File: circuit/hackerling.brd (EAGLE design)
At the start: 82.5 x 67.4 mm, 38 parts, among them IC1 MCP23017SP, IC2 MCP2300X/P, IC3 MIC5219BM5, SW2 SWITCH_B13EH, U1 MMA8452Q, U2 LCD-16X2NOSILK, U3 ARDUINOR3-BPLACE, U5 PCA9306, U7 POT

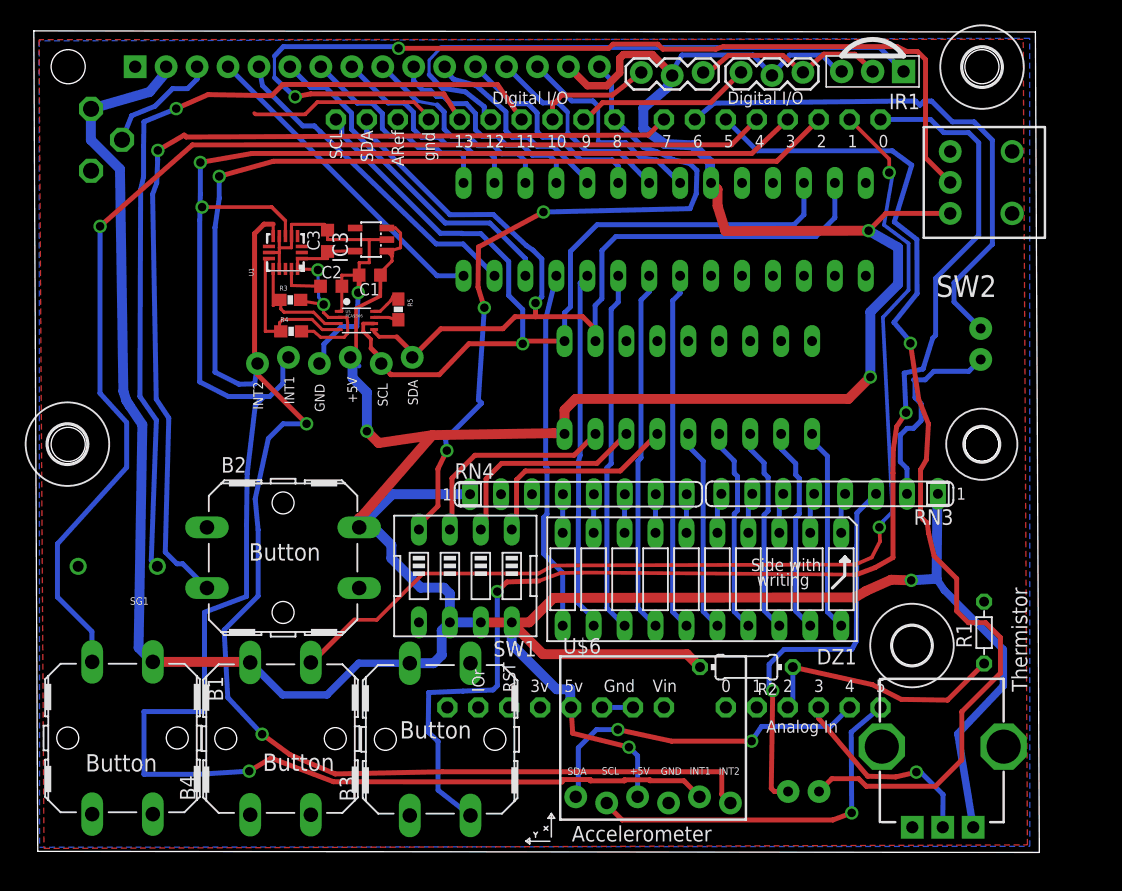
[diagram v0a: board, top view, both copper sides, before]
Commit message: changing accelerometer, adding hooked up address pins
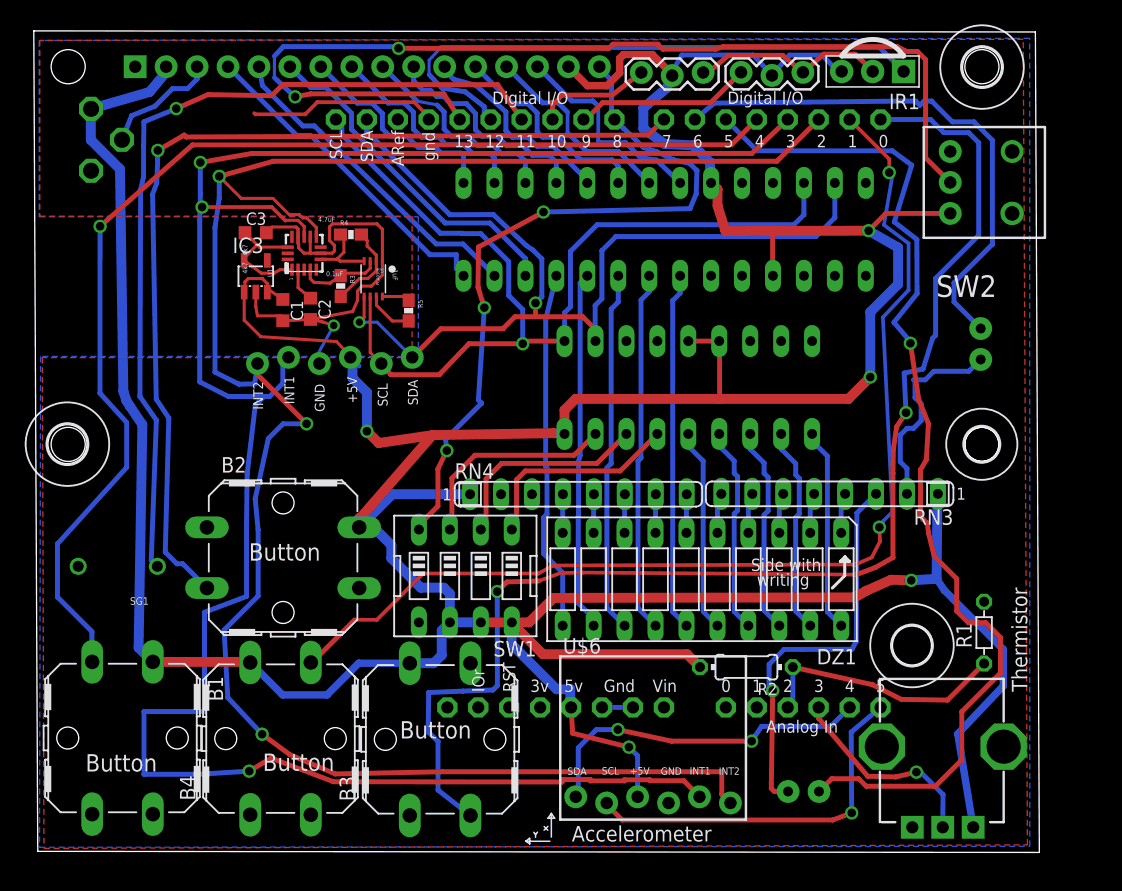
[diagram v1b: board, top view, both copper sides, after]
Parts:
- moved IC3 9.93 mm to (18.0, 48.5), turned to 0 degrees
- moved R4 9.34 mm to (25.8, 51.9)
- moved C1 7.70 mm to (20.2, 45.7), turned to 270 degrees
- moved C3 5.94 mm to (18.0, 52.0), turned to 0 degrees
- moved R3 4.29 mm to (24.9, 47.6), turned to 270 degrees
- moved U5 3.69 mm to (27.6, 48.2), turned to 180 degrees
- moved C2 2.51 mm to (22.5, 45.8), turned to 270 degrees
- moved U1 1.54 mm to (21.9, 50.3)
- moved R5 0.86 mm to (30.5, 45.6)
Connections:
- net GND: now also IC1.15, IC1.16, IC1.17, IC2.3, IC2.4
- net VCC: now also IC1.18, IC2.5, IC2.6
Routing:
- net VCC: track 379.8 -> 394.6 mm
- net SDA_3: track 13.6 -> 5.98 mm
- net GND: track 68.3 -> 74.7 mm
- net SDA: track 77.5 -> 81.4 mm, vias 1 -> 2
- net 3.3V: track 21.0 -> 17.3 mm, vias 2 -> 0
- net SCL_3: track 9.74 -> 6.79 mm
- net A_INT2: track 164.1 -> 161.7 mm
- net A_INT1: track 172.0 -> 173.7 mm
- net SCL: track 78.7 -> 80.2 mm
- net 5V: track 2.63 -> 3.90 mm
- net N$25: track 3.75 -> 2.81 mm
- net N$10: track 26.4 -> 27.1 mm
- net N$27: track 2.82 -> 2.29 mm
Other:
- board text added: "0.1uF"
- board text added: "1uF"
- board text added: "4.7uF"
- board text added: "4k7"

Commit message: adding adafruit libs to software folder
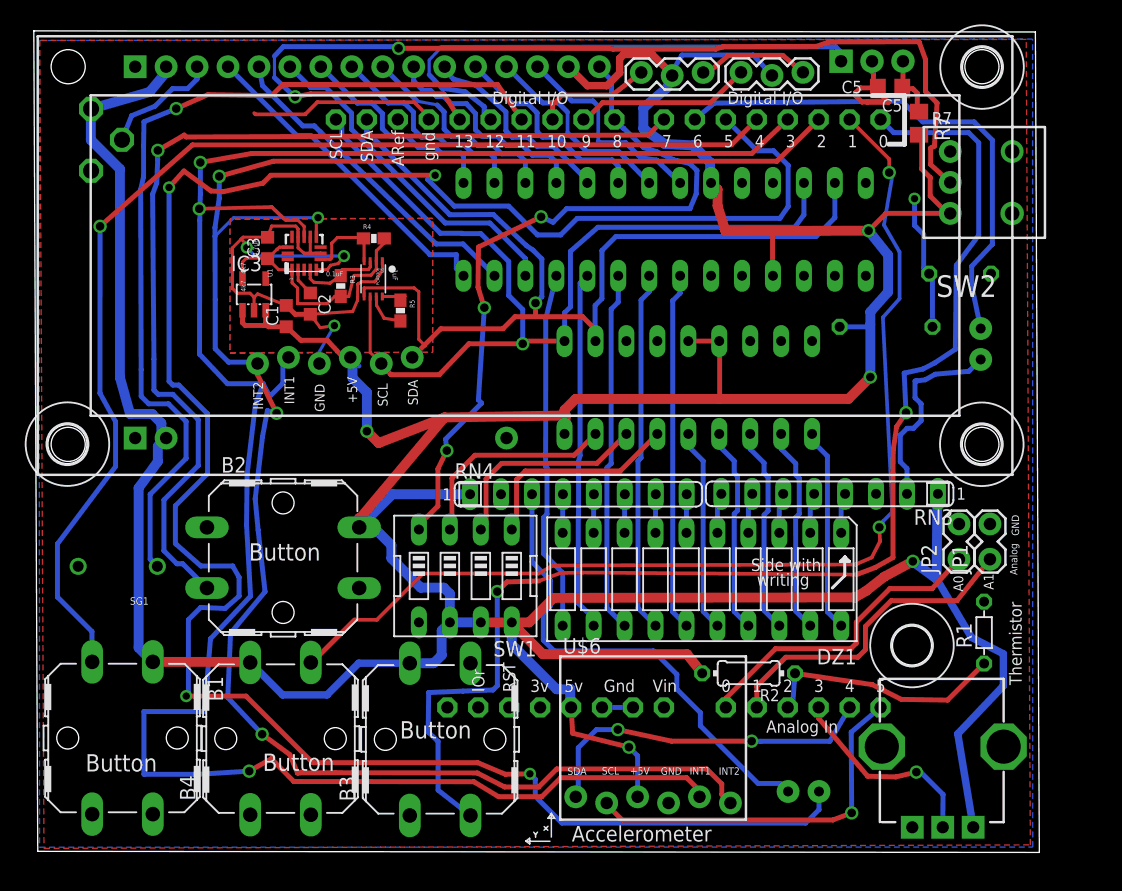
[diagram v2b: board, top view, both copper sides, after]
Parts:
- added C4: 10uF, rcl:C050-050X075
- added C5: (no value), resistor:C0805K
- added JP1, JP2: (no value), SparkFun:1X02_LOCK
- added R6: 47, resistor:0204/7
- added R7: (no value), rcl:R0805
- H1, H2, H3: value MOUNT-HOLE3.2 -> MOUNTHOLE'3.2; device holes:3,2 -> hackerscouts:HOLE_3.2
- H4: value MOUNT-HOLE2.8 -> MOUNTHOLE'3.2; device holes:2,8 -> hackerscouts:HOLE_3.2
- U2: value LCD-16X2NOSILK -> LCD_16X2; device SparkFun:LCD-16X2_NOSILK -> hackerscouts:LCD_16X2
- moved R4 1.91 mm to (27.7, 51.5)
- moved C3 1.59 mm to (18.9, 50.8), turned to 90 degrees
- moved IC3 1.50 mm to (17.8, 47.0)
- moved IR1 0.84 mm to (68.6, 66.1), flipped to the bottom
- moved R5 0.68 mm to (29.9, 45.6)
- moved C1 0.56 mm to (20.5, 45.2), turned to 90 degrees
- moved R2 0.54 mm to (58.4, 15.9)
- moved C2 0.42 mm to (22.5, 46.2)
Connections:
- new net N$19: C4.1, C5.1, IR1.3, R6.1, R7.1
- new net N$24: JP1.1, U3.A1
- new net N$26: JP2.1, U3.A0
- net GND: now also C4.2, C5.2, JP1.2, JP2.2, U2.B1
- net N$16: now also RN4.3; no longer RN3.3
- net N$2: now also U2.B13
- net VCC: now also R6.2, R7.2, U2.B2; no longer IR1.3
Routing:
- net IR_OUT1: track 86.2 -> 176.8 mm, vias 1 -> 4
- net N$24: track 0.00 -> 26.5 mm
- net N$26: track 0.00 -> 25.7 mm
- net N$19: track 0.00 -> 17.1 mm, vias 0 -> 1
- net GND: track 74.7 -> 86.6 mm, vias 1 -> 3
- net N$16: track 32.6 -> 39.4 mm, vias 1 -> 0
- net IR_IN: track 48.1 -> 43.1 mm
- net VCC: track 394.6 -> 399.5 mm
- net 3.3V: track 17.3 -> 22.0 mm
- net A_INT2: track 161.7 -> 157.3 mm, vias 3 -> 4
- net N$15: track 70.5 -> 74.5 mm
- net BTN2: track 80.5 -> 83.6 mm
- net SDA: track 81.4 -> 83.4 mm, vias 2 -> 1
- net IR_OUT2: track 44.2 -> 42.6 mm
- net BTN1: track 97.3 -> 96.1 mm
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- added copper zone on layer 1, net N$14
- added copper zone on layer 16, net N$14
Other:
- board text added: "A0"
- board text added: "A1"
- board text added: "Analog"
- board text added: "C4"
- board text added: "C5"
- board text added: "R6"
- board text added: "R7"

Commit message: old changes to circuit adding design docs adding libraries for new chips
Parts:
- added LED3: (no value), SparkFun:LED5MM
- R7: device rcl:R0805 -> rcl:R0603
- moved R7 3.78 mm to (72.5, 57.2)
- moved C5 2.61 mm to (70.6, 66.4)
- moved IR1 1.92 mm to (69.3, 64.3)
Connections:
- new net N$32: LED3.A, RN4.2
- net BTN3: now also B3.4; no longer B3.3
- net GND: now also B2.2, B3.1, SW1.6, SW1.7, SW1.8
- net IR_OUT1: now also LED3.K
- net N$3: now also U2.B12
- net VCC: no longer B1.1, B2.2, B3.2, B4.2, SW1.6, SW1.7, SW1.8
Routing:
- net VCC: track 399.5 -> 295.8 mm, vias 5 -> 4
- net N$32: track 0.00 -> 39.4 mm, vias 0 -> 3
- net BTN3: track 105.0 -> 77.2 mm
- net IR_OUT1: track 176.8 -> 185.7 mm, vias 4 -> 5
- net GND: track 86.6 -> 78.6 mm
- net N$19: track 17.1 -> 24.7 mm
- net IR_OUT2: track 42.6 -> 38.9 mm
- net IR_IN: track 43.1 -> 45.0 mm
- net N$12: track 16.6 -> 15.9 mm

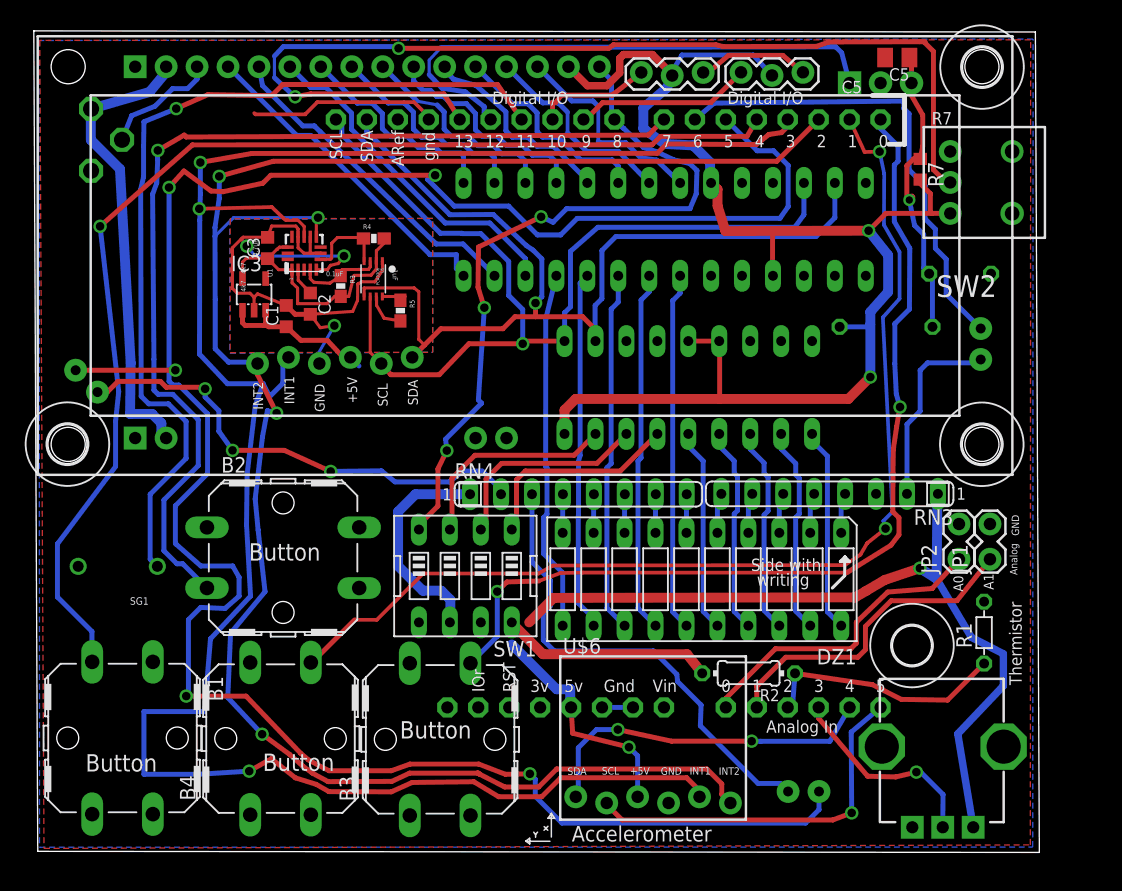
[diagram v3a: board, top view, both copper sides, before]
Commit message: tested LCD, works added library to test with - library needs cleaning made some minor changes to the board, removed rx, tx connections
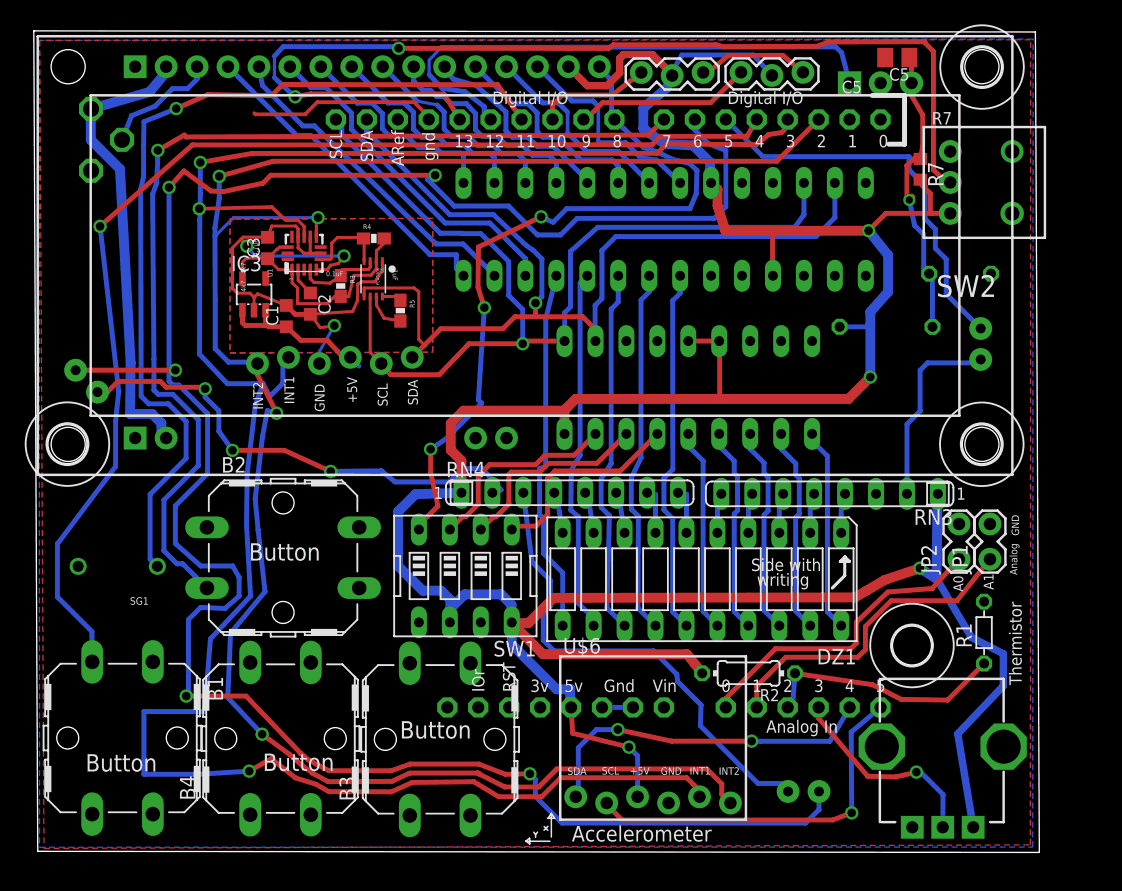
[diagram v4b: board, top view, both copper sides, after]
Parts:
- moved RN4 0.72 mm to (43.8, 30.7)
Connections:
- net BTN3: no longer U3.D0
- net BTN4: no longer U3.D1
- net GND: now also B1.2, B3.2, B4.1, B4.2
- net IR_OUT1: now also U3.D6; no longer U3.D5
- net IR_OUT2: now also U3.D5; no longer U3.D6
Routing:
- net BTN4: track 87.9 -> 0.00 mm, vias 2 -> 0
- net BTN3: track 77.2 -> 0.00 mm, vias 2 -> 0
- net VCC: track 295.8 -> 321.5 mm, vias 4 -> 5
- net IR_OUT1: track 185.7 -> 179.0 mm
- net IR_OUT2: track 38.9 -> 32.8 mm
- net DIP3: track 17.6 -> 16.6 mm
- net DIP2: track 17.4 -> 16.6 mm
- net N$23: track 3.19 -> 3.87 mm
- net N$28: track 3.18 -> 3.85 mm
- net N$32: track 39.4 -> 40.0 mm
- net BARGRAPH5: track 29.4 -> 30.0 mm
- net BACKLIGHT: track 60.2 -> 60.7 mm

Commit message: tested MCP23008, works changed buttons to connect to MCP23017 rerouted stuff
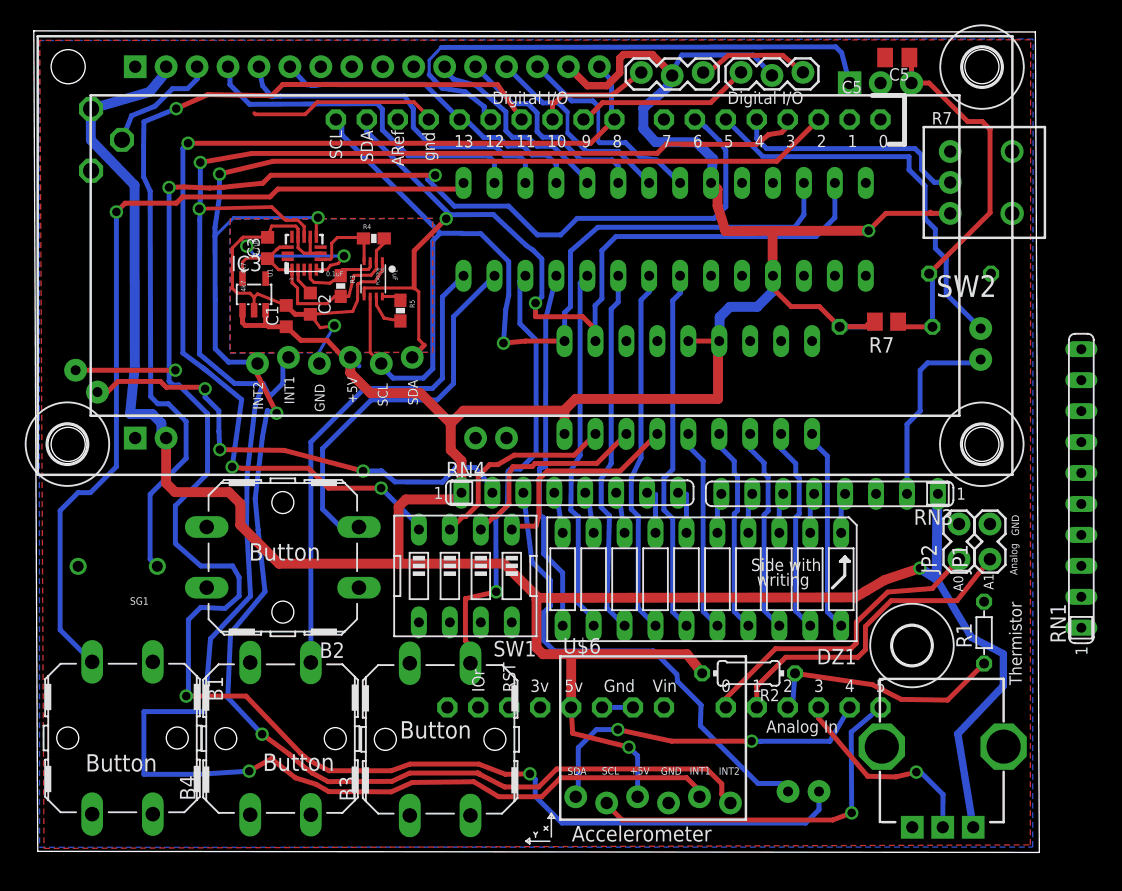
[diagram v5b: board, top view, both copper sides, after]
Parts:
- added RN1: (no value), resistor-sil:SIL10
- R7: device rcl:R0603 -> rcl:R0805
- moved R7 12.8 mm to (69.8, 44.7), turned to 180 degrees
- turned B2 to 180 degrees
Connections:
- removed net N$5: IC1.4, U2.10
- removed net N$6: IC1.3, U2.9
- removed net N$7: IC1.2, U2.8
- removed net N$8: IC1.1, U2.7
- removed net N$9: IC1.26, U2.6
- new net LCD_EN: IC1.4, U2.6, U3.D13
- net BTN1: now also IC1.1; no longer U3.D4
- net BTN2: now also IC1.27; no longer U3.D7
- net BTN3: now also IC1.26
- net BTN4: now also IC1.28
- net GND: now also B2.1
- net N$10: now also IC1.2; no longer IC1.28
- net N$11: now also IC1.3; no longer IC1.27
- net SWITCH: now also U3.D4; no longer U3.D13
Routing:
- net SWITCH: track 85.6 -> 19.9 mm, vias 2 -> 0
- net BTN2: track 83.6 -> 31.8 mm, vias 1 -> 0
- net BTN4: track 0.00 -> 40.2 mm
- net BTN3: track 0.00 -> 36.5 mm, vias 0 -> 1
- net N$9: track 28.8 -> 0.00 mm
- net BACKLIGHT: track 60.7 -> 88.1 mm
- net LCD_EN: track 0.00 -> 27.0 mm
- net BTN1: track 96.1 -> 70.0 mm
- net VCC: track 321.5 -> 341.5 mm, vias 5 -> 3
- net N$5: track 18.1 -> 0.00 mm
- net N$8: track 17.7 -> 0.00 mm
- net N$7: track 17.7 -> 0.00 mm
- net N$6: track 17.4 -> 0.00 mm
- net N$19: track 24.7 -> 31.6 mm, vias 1 -> 0
- net SCL: track 80.2 -> 84.7 mm
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
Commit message: circuit state upon submit of version 1.0
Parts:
- removed RN1: (no value), resistor-sil:SIL10
- moved C5 3.91 mm to (70.7, 62.5)
- moved C1 1.20 mm to (20.4, 44.0)
- moved C2 1.20 mm to (22.4, 45.0)
- moved H1 1.20 mm to (2.49, 33.5)
- moved H3 1.20 mm to (77.6, 64.4)
- moved IC3 1.20 mm to (17.8, 45.8)
- moved LED2 1.20 mm to (77.5, 41.7)
- moved LED3 1.20 mm to (4.06, 38.6)
- moved R5 1.20 mm to (29.8, 44.4)
- moved SERVO1 1.20 mm to (57.8, 63.9)
- moved SW1 1.20 mm to (35.1, 22.6)
- moved U5 1.20 mm to (27.6, 47.0)
- moved C3 1.20 mm to (18.9, 49.6)
- moved U1 1.20 mm to (21.9, 49.1)
- moved B1 1.20 mm to (7.01, 9.35)
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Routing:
- net GND: track 78.6 -> 84.4 mm
- net N$19: track 31.6 -> 32.9 mm
- net IR_IN: track 45.0 -> 43.6 mm
- net BTN3: track 36.5 -> 35.9 mm
- net TEMP: track 20.1 -> 20.6 mm
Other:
- board text added: "+"
- board text added: "-"
- board text added: "1.0"
- board text added: "16:"
- board text added: "200k"
- board text added: "Circuit"
- board text added: "For information about"
- board text added: "Hackerling"
- board text added: "Install resistor arrays"
- board text added: "Install switch"
- board text added: "LED1"
- board text added: "LED2"
- board text added: "LED3"
- board text added: "Leave .25" out"
- board text added: "PWM"
- board text added: "Solder on this side."
- board text added: "Speaker"
- board text added: "Step 12:"
- board text added: "Step 13:"
- board text added: "Step 14:"
- board text added: "Step 15"
- board text added: "Step 17:"
- board text added: "Step 18:"
- board text added: "Step 19:"
- board text added: "Step 20:"
- board text added: "Step 21:"
- board text added: "Step 22:"
- board text added: "Step 3: Install Arduino headers, pointing down."
- board text added: "Step 5"
- board text added: "Step 6"
- board text added: "Step 9:"
- board text added: "go to:"
- board text added: "match up"
- board text added: "or the Hacker Scouts"
- board text added: "pointing down"
- board text added: "program,"
- board text added: "the indent"
- board text added: "this circuit,"
- board text added: "v"
- board text added: "www.hacker-scouts.org"
- board text removed: "??:"
- board text removed: "Install LED"
- board text removed: "Install resistor array"
- board text removed: "Install switch here"
- board text removed: "Leave .5" out"
- board text removed: "Solder on the"
- board text removed: "Step 3: Install Arduino headers. Solder other side."
- board text removed: "Step 5:"
- board text removed: "Step 6:"
- board text removed: "Step 9: Servo headers."
- board text removed: "Step ??"
- board text removed: "Step ??:"
- board text removed: "match up the indent"
- board text removed: "only use 5 pins"
- board text removed: "other side."
